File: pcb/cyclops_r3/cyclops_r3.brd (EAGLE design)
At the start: 69.8 x 53.3 mm, 113 parts, among them M12_TUBE_MOUNT PT-LH001, Q1 SUM11006, Q2 IRF540, U1 MCP4921, U10 AD829, U11 MIC5225, U12 MIC5270, U2 317-N, U3 TLV37, U4 337-N, U5 ADR03, U6 OP1177, U7 TLV2374, U8 ZXTD45, U9 ADA4899

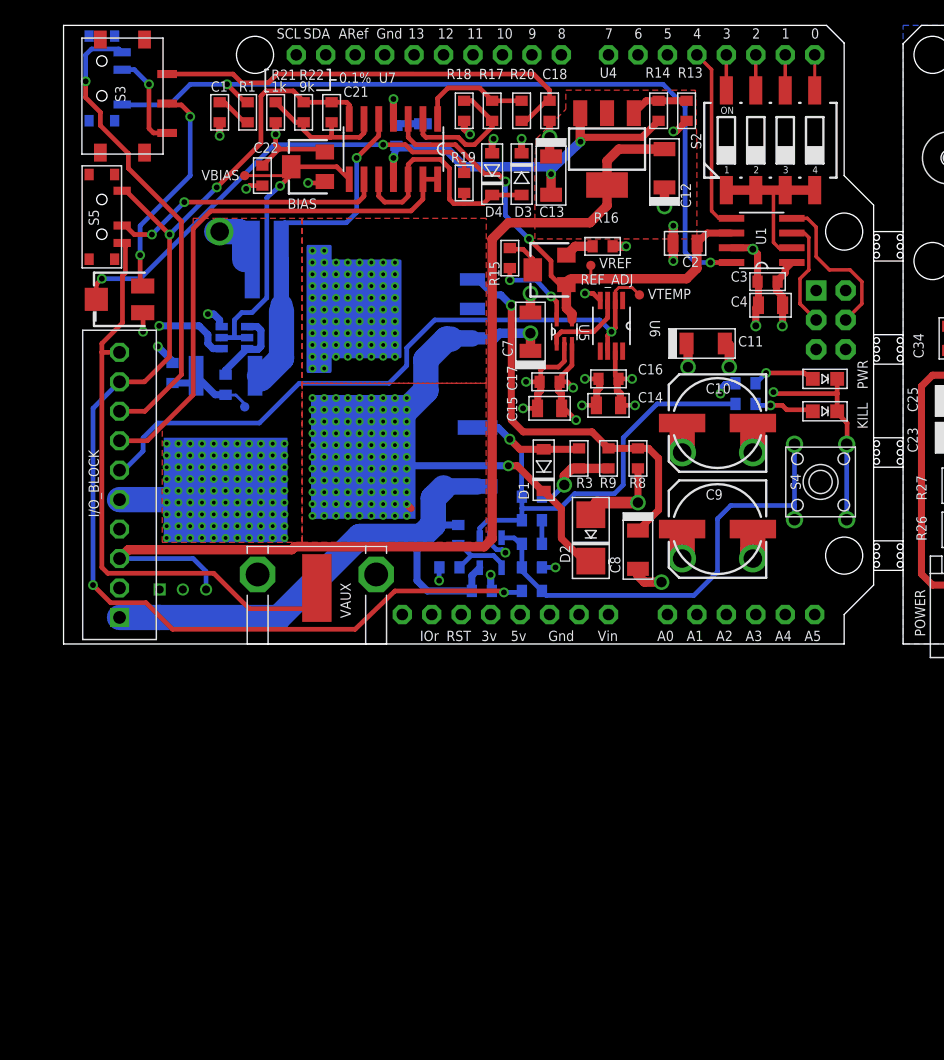
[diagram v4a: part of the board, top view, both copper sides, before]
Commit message: More revisions due to circuit assembly and UI considerations. More design notes.
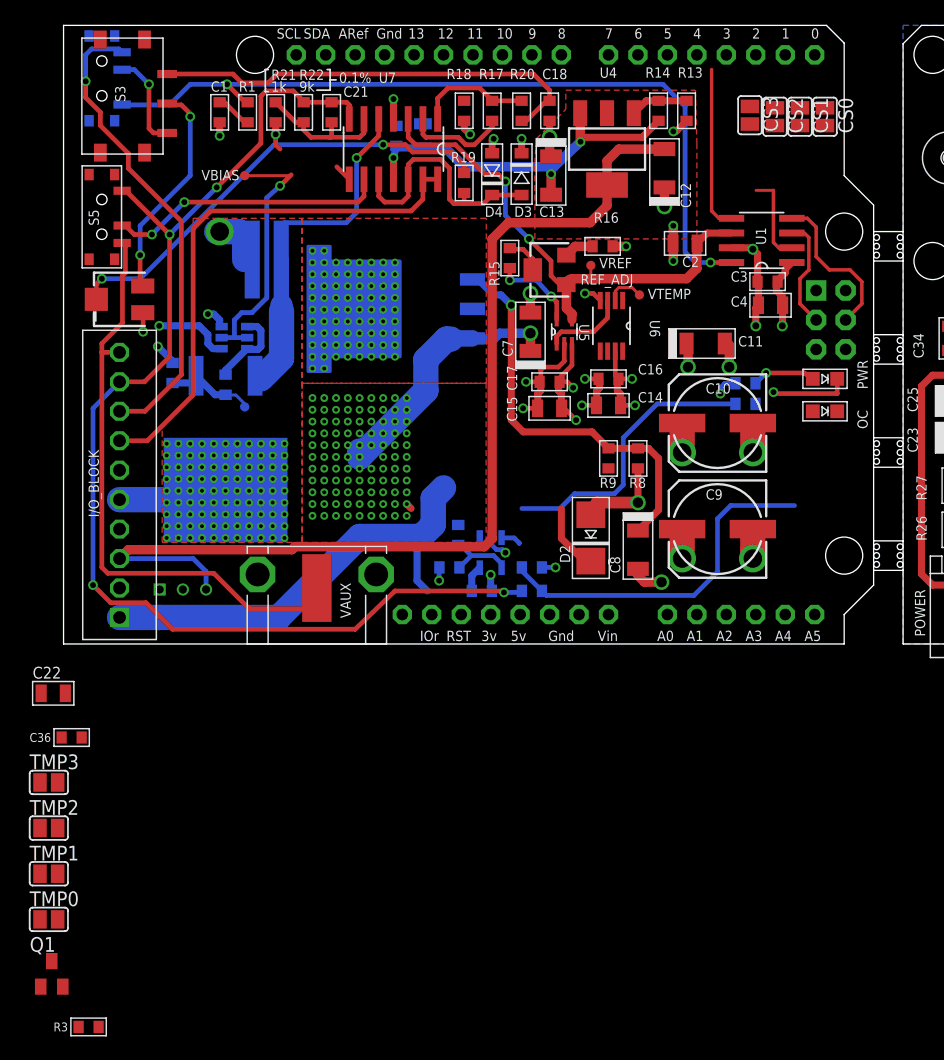
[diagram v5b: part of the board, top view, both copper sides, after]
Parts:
- removed BIAS: 10k, cyclops:SM-42/43W
- removed D1: MMSZ, cyclops:SOD123
- removed R10: 220k, cyclops:0603
- removed R6: 91k, cyclops:0603
- removed R7: 1k, cyclops:0603
- removed S2: 219-04, cyclops:CTS-219-04
- removed S4: REVIVE, jonnew-eagle:B3F
- added C36: .1uF, cyclops:0603
- added CS0, CS1, CS2, CS3, TMP0, TMP1, TMP2, TMP3: (no value), cyclops:SJ
- C22: value .1uF -> 1uF; device cyclops:0603 -> cyclops:0805
- C5: value 10nF -> 0.1uF
- Q1: value SUM11006 -> BC817-16SMD; device cyclops:TO-262_01 -> cyclops:SOT23-BEC
- R11: value 3k -> 1k
- R2: value 100k -> 10k
- R4: value 56k -> 110k
- R5: value 4k -> 10k
- U3: value TLV37 -> TLV3701
- moved R3 64.7 mm to (0.89, -33.0), turned to 0 degrees
- moved Q1 54.5 mm to (-2.29, -28.4), flipped to the top, turned to 0 degrees
- moved C22 48.1 mm to (-2.16, -4.25), turned to 0 degrees
- renumbered KILL to OC
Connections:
- removed net +15V_ON: C7.+, D1.C, D2.C, Q1.D, U2.3
- removed net KILL: D1.A, Q1.G, R10.2, R11.2, R3.2, R7.1, U3.1
- removed net N$2 (its old number): Q2.S, RSENSE.2, U7.5
- new net CS4: ARDUNIO.A0, TMP0.1
- new net CS5: ARDUNIO.A1, TMP1.1
- new net CS6: ARDUNIO.A3, TMP3.1
- new net CS8: ARDUNIO.A2, TMP2.1
- new net LED+: Q2.S
- new net N$27: R3.2, U3.1
- new net N$28: Q1.B, R3.1
- net +12V: now also C6.1, Q2.D, R11.2, R4.1, U3.5; no longer BIAS.1, C22.1
- net +15V: now also C7.+, D2.C, U2.3; no longer C6.1, Q1.S, R4.1, U3.5
- net -2.1V: now also C22.1, C36.1; no longer C19.2, C20.2
- net AGND: now also C19.2, C20.2, C22.2, C36.2, Q1.E
- net COMP+: no longer R6.2, S4.1, S4.2
- net CS: now also CS0.2, CS1.2, CS2.2, CS3.2; no longer S2.1, S2.2, S2.3, S2.4
- net CS0: now also ARDUNIO.D2, CS0.1; no longer ARDUNIO.D0, S2.5
- net CS1: now also ARDUNIO.D3, CS1.1; no longer ARDUNIO.D1, S2.6
- net CS2: now also ARDUNIO.D4, CS2.1; no longer ARDUNIO.D2, S2.7
- net CS3: now also ARDUNIO.D5, CS3.1; no longer ARDUNIO.D3, S2.8
- net GND: no longer BIAS.3, C22.2, OC.C, R10.1, R3.1, S4.3, S4.4
- net LDAC: now also ARDUNIO.D6; no longer ARDUNIO.D4
- net LED-: now also RSENSE.2, U7.5; no longer Q2.D
- net N$4: no longer BIAS.2
- net N$9: now also OC.C, Q1.C; no longer R6.1, R7.2
- net TEMP: now also TMP0.2, TMP1.2, TMP2.2, TMP3.2
- net VTEMP: no longer I/O_BLOCK.P$6
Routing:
- net VTEMP: track 57.7 -> 3.28 mm, vias 1 -> 0
- net +15V_ON: track 49.4 -> 0.00 mm, vias 101 -> 0
- net KILL: track 46.5 -> 0.00 mm, vias 1 -> 0
- net N$2 (its old number): track 30.3 -> 0.00 mm, vias 1 -> 0
- net LED-: track 8.32 -> 37.6 mm
- net GND: track 102.7 -> 78.1 mm, vias 32 -> 31
- net +12V: track 68.1 -> 88.5 mm, vias 90 -> 89
- net +15V: track 50.4 -> 70.0 mm, vias 0 -> 99
- net COMP+: track 41.1 -> 32.3 mm
- net CS: track 15.4 -> 7.77 mm
- net N$2: track 5.33 -> 0.00 mm, vias 1 -> 0
- net N$4: track 29.2 -> 24.5 mm
- net N$8: track 12.0 -> 8.83 mm
- net CS3: track 3.07 -> 0.00 mm
- net CS2: track 3.07 -> 0.00 mm
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- added copper zone on layer 1, net +15V
- removed copper zone on layer 1, net +15V_ON

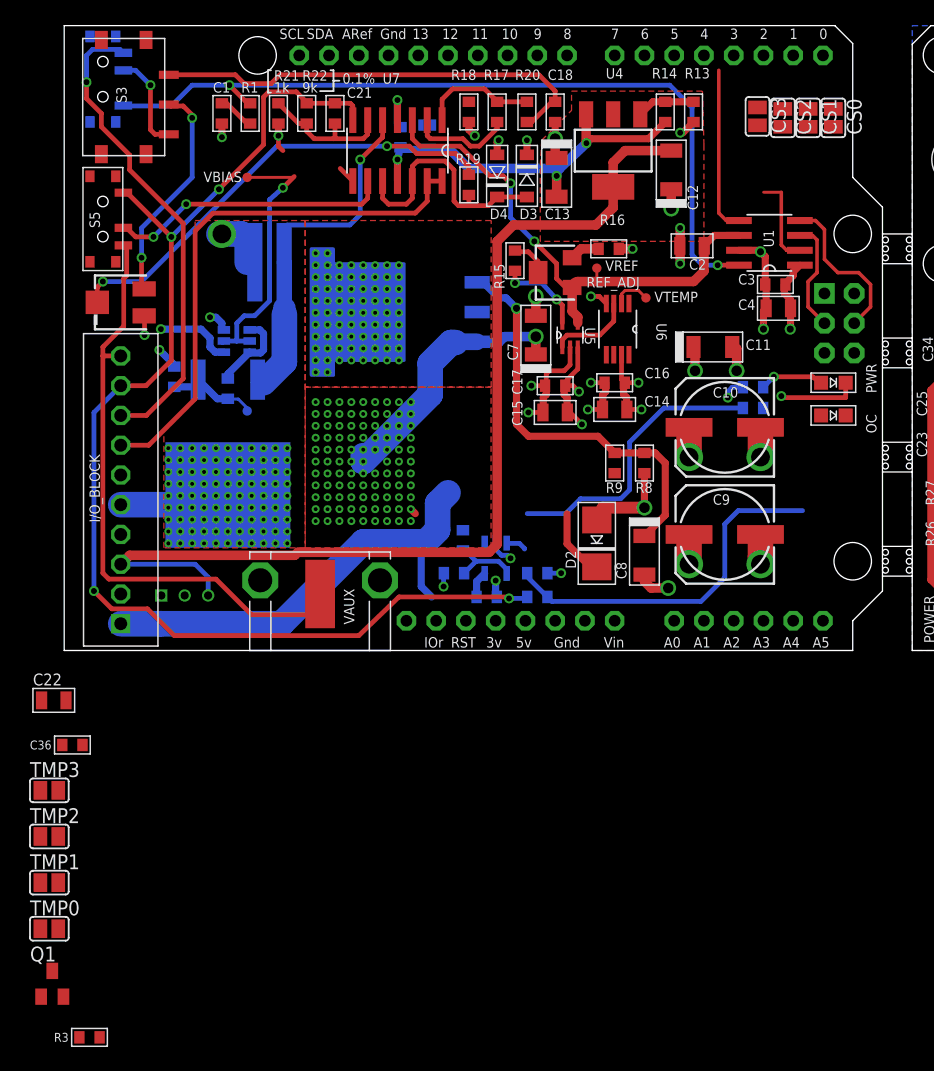
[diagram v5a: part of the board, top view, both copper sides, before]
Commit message: Making fixes based on previous assembly.
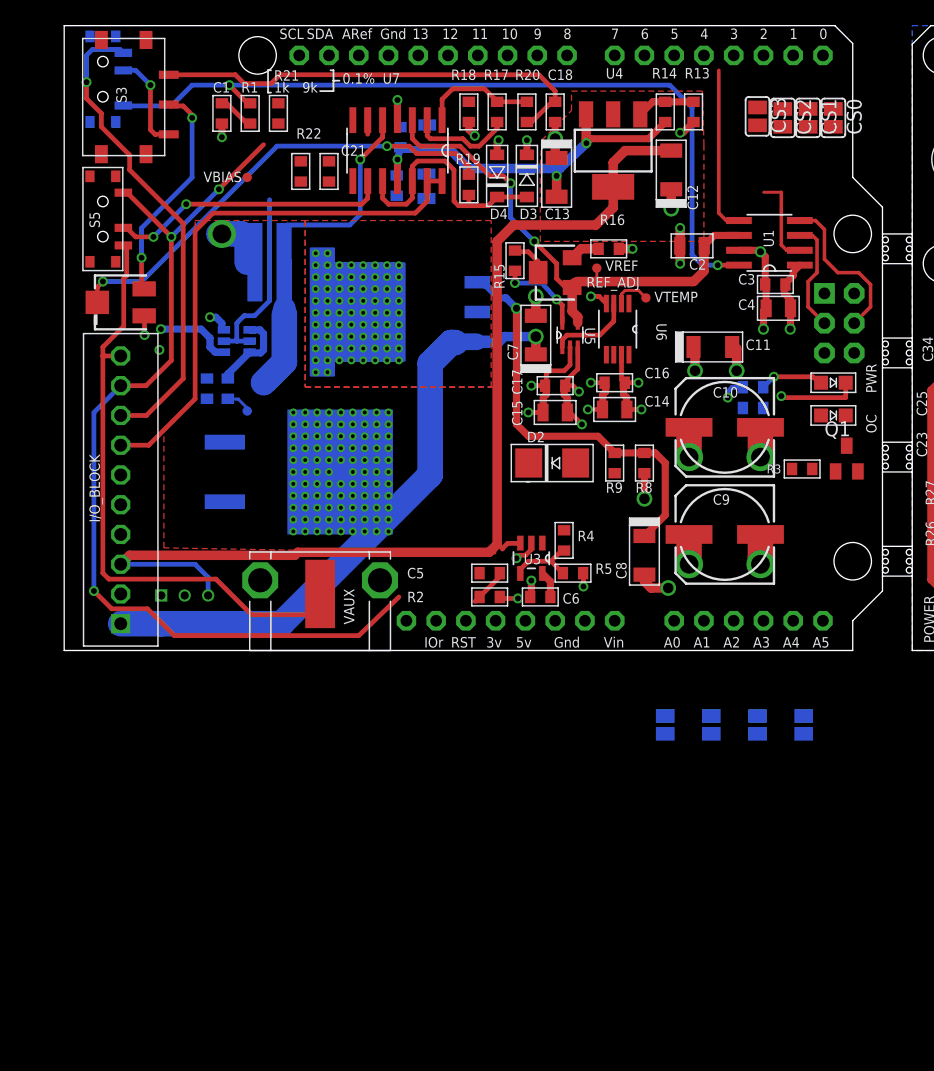
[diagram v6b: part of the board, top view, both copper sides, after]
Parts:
- moved Q1 81.3 mm to (65.5, 16.4)
- moved R3 77.8 mm to (61.7, 15.5)
- moved TMP3 64.6 mm to (61.8, -6.35), flipped to the bottom, turned to 90 degrees
- moved TMP2 61.2 mm to (57.9, -6.35), flipped to the bottom, turned to 90 degrees
- moved TMP1 58.1 mm to (54.0, -6.35), flipped to the bottom, turned to 90 degrees
- moved TMP0 55.4 mm to (50.0, -6.35), flipped to the bottom, turned to 90 degrees
- moved C36 55.2 mm to (27.1, 39.7), flipped to the bottom, turned to 270 degrees
- moved C22 54.2 mm to (29.7, 39.6), flipped to the bottom, turned to 270 degrees
- moved R5 10.2 mm to (42.2, 6.60), flipped to the top
- moved R4 8.64 mm to (41.4, 9.40), flipped to the top
- moved D2 7.85 mm to (40.4, 16.0), turned to 180 degrees
- moved Q2 5.68 mm to (17.8, 15.2), turned to 90 degrees
- moved C21 4.98 mm to (21.3, 40.9)
- moved R22 4.98 mm to (18.9, 40.9)
- moved C6 4.57 mm to (39.4, 4.57), flipped to the top
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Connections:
- net +12V: no longer I/O_BLOCK.P$4
- net GND: now also I/O_BLOCK.P$6
- net LED+: now also I/O_BLOCK.P$4
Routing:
- net +12V: track 88.5 -> 52.7 mm, vias 89 -> 88
- net COMP+: track 32.3 -> 5.05 mm
- net VI: track 104.7 -> 81.6 mm
- net +15V: track 70.0 -> 54.4 mm, vias 99 -> 1
- net N$15: track 12.0 -> 1.20 mm
- net N$4: track 24.5 -> 16.1 mm, vias 1 -> 0
- net LED-: track 37.6 -> 29.8 mm
- net N$13: track 8.04 -> 2.23 mm
- net GND: track 78.1 -> 72.5 mm, vias 31 -> 29
- removed copper zone on layer 1, net +15V
- removed copper zone on layer 2, net N$14

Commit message: Started udating layout and parts for r3.1
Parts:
- removed CTL_K: 1k, cyclops:SM-42/43A
- removed I/O_BLOCK: SCREW10_0.1-THRU, cyclops:SCREW10
- added GAIN: 1k, cyclops:SM-42/43A
- added PWR_DIST: PINH2X6, cyclops:2X06-BIG
- added REF-2.5: TPTP08R, cyclops:TP08R
- added U$1: PINH1X2_SABRE-2, cyclops:SABRE-2
- added U$2: PINH1X3_SABRE-3, cyclops:SABRE-3
- added VAUX1, VCTL, VI: 361V509E, cyclops:361V509E
- ARDUNIO: value ARDUINO_R3_ICSP -> ARDUINO_R3_ICSP_PINS; device cyclops:ARDUINOR3_ICSP -> cyclops:ARUDINOR3_PINS
- VREF: value TPTP08R -> 361V509E; device cyclops:TP08R -> cyclops:361V509E
- moved R13 140.3 mm to (-75.1, 104.5), turned to 0 degrees
- moved R14 137.1 mm to (-75.1, 102.1), turned to 180 degrees
- moved C12 135.5 mm to (-70.1, 102.6), turned to 180 degrees
- moved C2 135.4 mm to (-63.6, 104.4), turned to 270 degrees
- moved U4 129.6 mm to (-71.8, 97.7), turned to 270 degrees
- moved VTEMP 128.5 mm to (-59.2, 100.5), turned to 90 degrees
- moved R8 125.8 mm to (-45.1, 100.3), turned to 0 degrees
- moved R16 125.5 mm to (-63.4, 97.3), turned to 270 degrees
- moved C18 124.8 mm to (-75.1, 92.7), turned to 0 degrees
- moved U6 124.5 mm to (-56.5, 98.0), turned to 0 degrees
- moved C24 123.2 mm to (137.7, 117.9)
- moved C26 123.2 mm to (149.4, 138.6)
- moved C31 123.2 mm to (139.0, 134.7)
- moved C34 123.2 mm to (133.9, 134.7)
- moved D5 123.2 mm to (143.8, 150.2)
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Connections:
- removed net AGND: C19.2, C20.2, C22.2, C23.-, C24.2, C25.+, C27.2, C28.2, C29.2, C30.2, C31.2, C32.2, C33.2, C34.2, C35.2, C36.2, GND.TP, POWER.2, Q1.E, R27.2, R30.1, U11.2, U12.2, VPD.2, VPD.3
- net +15V: now also PWR_DIST.1, PWR_DIST.2, PWR_DIST.3, PWR_DIST.4, U$2.1A, U$2.1B; no longer I/O_BLOCK.P$1
- net -6V: now also PWR_DIST.10, PWR_DIST.11, PWR_DIST.12, PWR_DIST.9, U$2.3A, U$2.3B; no longer I/O_BLOCK.P$3
- net GND: now also C19.2, C20.2, C22.2, C23.-, C24.2, C25.+, C27.2, C28.2, C29.2, C30.2, C31.2, C32.2, C33.2, C34.2, C35.2, C36.2, GAIN.3, GND.TP, POWER.2, PWR_DIST.5, PWR_DIST.6, PWR_DIST.7, PWR_DIST.8, Q1.E, R27.2, R30.1, U$2.2A, U$2.2B, U11.2, U12.2, VAUX1.2, VAUX1.3, VCTL.2, VCTL.3, VI.2, VI.3, VPD.2, VPD.3, VREF.2, VREF.3; no longer CTL_K.3, I/O_BLOCK.P$2, I/O_BLOCK.P$6
- net LED+: now also U$1.1A, U$1.1B; no longer I/O_BLOCK.P$4
- net LED-: now also U$1.2A, U$1.2B; no longer I/O_BLOCK.P$5
- net N$7: now also GAIN.2; no longer CTL_K.2
- net REFA: now also REF-2.5.TP; no longer VREF.TP
- net VAUX: now also VAUX1.1; no longer I/O_BLOCK.P$10
- net VCTL: now also GAIN.1, VCTL.1; no longer CTL_K.1
- net VI: now also VI.1; no longer I/O_BLOCK.P$9
- net VINPUT: no longer I/O_BLOCK.P$8
- net VREF: now also VREF.1; no longer I/O_BLOCK.P$7
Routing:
- net -6V: track 119.5 -> 31.0 mm
- net VI: track 81.6 -> 0.00 mm, vias 4 -> 0
- net DACA: track 69.6 -> 0.00 mm, vias 2 -> 0
- net VAUX: track 54.9 -> 0.00 mm
- net +15V: track 54.4 -> 0.00 mm, vias 1 -> 0
- net VREF: track 46.2 -> 0.00 mm
- net REFA: track 45.8 -> 0.00 mm, vias 2 -> 0
- net GND: track 72.5 -> 26.8 mm, vias 29 -> 15
- net +12V: track 52.7 -> 9.71 mm, vias 88 -> 0
- net VINPUT: track 41.1 -> 0.00 mm, vias 1 -> 0
- net N$7: track 39.5 -> 0.00 mm, vias 2 -> 0
- net REFA2X: track 38.2 -> 0.00 mm
- net N$72: track 35.2 -> 0.00 mm, vias 1 -> 0
- net -2.1V: track 31.0 -> 0.00 mm, vias 3 -> 0
- net LED-: track 29.8 -> 0.00 mm, vias 99 -> 0
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- removed copper zone on layer 15, net +12V
- removed copper zone on layer 15, net +5V
- removed copper zone on layer 2, net AGND
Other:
- board size 69.8 x 53.3 mm -> 157.7 x 161.7 mm

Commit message: Lots of changes. Started proper layout of 3.2.
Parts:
- removed S1: INPUT SRC, cyclops:PCM12
- removed U$1: PINH1X2_SABRE-2, cyclops:SABRE-2
- removed U$2: PINH1X3_SABRE-3, cyclops:SABRE-3
- added INPUT: (no value), cyclops:JS102011SAQN
- added LED: PINH1X2_S2B-PH-K-S, cyclops:S2B-PH-K-S
- added PWR_IN: PINH1X3_SABRE-3, cyclops:SABRE-3
- GAIN: value 1k -> 296X; device cyclops:SM-42/43A -> cyclops:296X-POT
- OC, PWR: device cyclops:CHIP-LED0805 -> cyclops:LED-0603
- PD_POWER: device cyclops:S2B-PH-K-S -> cyclops:S3B-PH-K-S
- POWER: device cyclops:S2B-PH-K-S -> cyclops:SCREW3
- S5: device cyclops:PCM12 -> cyclops:JS102011SAQN
- moved U4 193.6 mm to (109.3, 29.3)
- moved R14 192.7 mm to (103.4, 29.3), turned to 90 degrees
- moved R13 192.3 mm to (103.4, 32.8), turned to 90 degrees
- moved C12 191.4 mm to (108.7, 34.3), turned to 0 degrees
- moved C13 190.3 mm to (108.1, 24.5), turned to 180 degrees
- moved C7 168.5 mm to (96.1, 18.7), turned to 270 degrees
- moved C1 164.2 mm to (86.4, 33.8), turned to 90 degrees
- moved R1 162.3 mm to (83.9, 33.8), turned to 270 degrees
- moved R21 160.4 mm to (81.5, 33.8), turned to 90 degrees
- moved D2 159.7 mm to (100.5, 26.7)
- moved VBIAS 156.1 mm to (84.2, 39.2), turned to 0 degrees
- moved C19 153.7 mm to (73.2, 31.8), flipped to the top, turned to 0 degrees
- moved R22 153.1 mm to (79.6, 38.7), turned to 270 degrees
- moved R9 152.7 mm to (89.2, 25.0), turned to 90 degrees
- moved R8 152.2 mm to (89.2, 28.6), turned to 90 degrees
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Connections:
- removed net 3V: ARDUNIO.3V
- removed net VIN: ARDUNIO.VIN
- net +12V: now also ARDUNIO.VIN, POWER.P$1; no longer POWER.1
- net +15V: now also PWR_IN.1A, PWR_IN.1B; no longer U$2.1A, U$2.1B
- net +5V: now also ARDUNIO.5VA; no longer ARDUNIO.+5V, ARDUNIO.5V
- net -6V: now also POWER.P$3, PWR_IN.3A, PWR_IN.3B; no longer POWER.3, U$2.3A, U$2.3B
- net DACA: now also INPUT.1; no longer S1.1
- net GND: now also ARDUNIO.GND1, ARDUNIO.GND2, GAIN.E, POWER.P$2, PWR_IN.2A, PWR_IN.2B; no longer ARDUNIO.GND, ARDUNIO.GND$1, ARDUNIO.GND$2, ARDUNIO.GND$3, GAIN.3, POWER.2, U$2.2A, U$2.2B
- net LED+: now also LED.1; no longer U$1.1A, U$1.1B
- net LED-: now also LED.2; no longer U$1.2A, U$1.2B
- net N$7: now also GAIN.W; no longer GAIN.2
- net VCTL: now also GAIN.A; no longer GAIN.1, VCTL.1
- net VCTL_PRE: now also INPUT.2; no longer S1.2
- net VINPUT: now also INPUT.3, VCTL.1; no longer S1.3
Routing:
- net CS: track 0.00 -> 32.1 mm
- net LDAC: track 0.00 -> 24.7 mm
- net SDI: track 0.00 -> 15.8 mm
- net REFA: track 0.00 -> 13.1 mm
- net SCLK: track 0.00 -> 12.6 mm
- net GND: track 26.8 -> 36.2 mm, vias 15 -> 19
- net +5V: track 0.00 -> 5.42 mm, vias 0 -> 2
- net -6V: track 31.0 -> 35.6 mm
- net CS3: track 0.00 -> 2.93 mm
- net CS2: track 0.00 -> 2.93 mm
- net CS1: track 0.00 -> 2.93 mm
- net CS0: track 0.00 -> 2.93 mm
- net +12V: track 9.71 -> 11.5 mm, vias 0 -> 59
- added copper zone on layer 15, net +12V
- added copper zone on layer 16, net +12V
- added copper zone on layer 15, net +15V
- added copper zone on layer 15, net +5V
- added copper zone on layer 16, net -6V
- added copper zone on layer 15, net KEEPOUT
- added copper zone on layer 2, net KEEPOUT
- removed copper zone on layer 1, net -6V
- removed copper zone on layer 1, net LED-
